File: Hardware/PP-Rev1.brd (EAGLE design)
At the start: 100 x 80 mm, 113 parts, among them IC1 LT6004, Q1 MOSFET-PCHANNEL, Q2 MOSFET-PCHANNEL, Q3 MOSFET-PCHANNEL, Q4 MOSFET-PCHANNEL, Q5 MOSFET-PCHANNEL, Q6 MOSFET-PCHANNEL, Q7 MOSFET-PCHANNEL, Q8 MOSFET-PCHANNEL, Q9 CSD18532

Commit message: Added E-Stop connectors, powersupplies (12V, 5V), additional cell tap line connector for off-board measurements
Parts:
- added C17, C18, C19, C20: 47µF, resistor:C1206
- added CELL-MEAS: 22-23-2091, con-molex:22-23-2091
- added F1: PTCSMD, SparkFun-PowerIC:PTC-1206
- added JP2, JP3: M02POLAR, SparkFun-Connectors:MOLEX-1X2
- added L2, L3: Fair-Rite 2773019447, rcl:L8530M
- added OKI-78SR: Q_OKI-78SR5, MRDT-2015-PowerBoard:OKI-78SRH
- added OKI-78SR1: Q_OKI-78SR12, MRDT-2015-PowerBoard:OKI-78SRH
- added R45, R46: 10kΩ, resistor:R1206
- added S1: (no value), SparkFun-Electromechanical:SWITCH-SPDT
- moved CHARGER+ 204.5 mm to (90.2, 11.4)
- moved U$12 178.6 mm to (40.6, 20.3)
- moved U$9 163.5 mm to (47.0, 26.7)
- moved U$11 159.1 mm to (71.1, 12.7), turned to 90 degrees
- moved Q9 155.0 mm to (57.1, 11.4), turned to 270 degrees
- moved U$4 124.4 mm to (31.8, 53.3), turned to 90 degrees
- moved U$10 123.3 mm to (72.4, 31.8), turned to 90 degrees
- moved CHARGER- 114.6 mm to (90.2, 34.3)
- moved U$5 97.1 mm to (38.1, 43.2), turned to 180 degrees
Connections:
- removed net N$32: C14.1, IRLS3034-7P.2.PAD, IRLS3034-7P.PAD, R41.2, U$2.5_1, U$2.5_10, U$2.5_11, U$2.5_12, U$2.5_13, U$2.5_14, U$2.5_15, U$2.5_16, U$2.5_2, U$2.5_3, U$2.5_4, U$2.5_5, U$2.5_6, U$2.5_7, U$2.5_8, U$2.5_9, U$2.5_B, U$2.5_T, U$4.4_1, U$4.4_10, U$4.4_11, U$4.4_12, U$4.4_13, U$4.4_14, U$4.4_15, U$4.4_16, U$4.4_2, U$4.4_3, U$4.4_4, U$4.4_5, U$4.4_6, U$4.4_7, U$4.4_8, U$4.4_9, U$4.4_B, U$4.4_T, U$8.6, U$8.8
- new net 5V: C18.1, L3.2, R45.2, R46.2
- new net ESTOP_1: JP3.2, R45.1
- new net ESTOP_2: JP2.2, R46.1
- new net LOGIC_POWER: F1.2, OKI-78SR.1, OKI-78SR1.1
- new net N$100: C17.1, L3.1, OKI-78SR.3
- new net N$33: C19.1, L2.1, OKI-78SR1.3
- new net N$41: C14.1, IRLS3034-7P.2.PAD, IRLS3034-7P.PAD, R41.2, S1.1, U$2.5_1, U$2.5_10, U$2.5_11, U$2.5_12, U$2.5_13, U$2.5_14, U$2.5_15, U$2.5_16, U$2.5_2, U$2.5_3, U$2.5_4, U$2.5_5, U$2.5_6, U$2.5_7, U$2.5_8, U$2.5_9, U$2.5_B, U$2.5_T, U$4.4_1, U$4.4_10, U$4.4_11, U$4.4_12, U$4.4_13, U$4.4_14, U$4.4_15, U$4.4_16, U$4.4_2, U$4.4_3, U$4.4_4, U$4.4_5, U$4.4_6, U$4.4_7, U$4.4_8, U$4.4_9, U$4.4_B, U$4.4_T, U$8.6, U$8.8
- new net N$42: F1.1, S1.2
- net +12V: now also C20.1, L2.2
- net CELL_1: now also CELL-MEAS.8
- net CELL_2: now also CELL-MEAS.7
- net CELL_3: now also CELL-MEAS.6
- net CELL_4: now also CELL-MEAS.5
- net CELL_5: now also CELL-MEAS.4
- net CELL_6: now also CELL-MEAS.3
- net CELL_7: now also CELL-MEAS.2
- net CELL_8: now also CELL-MEAS.1
- net GND: now also C17.2, C18.2, C19.2, C20.2, CELL-MEAS.9, JP2.1, JP3.1, OKI-78SR.2, OKI-78SR1.2, S1.3

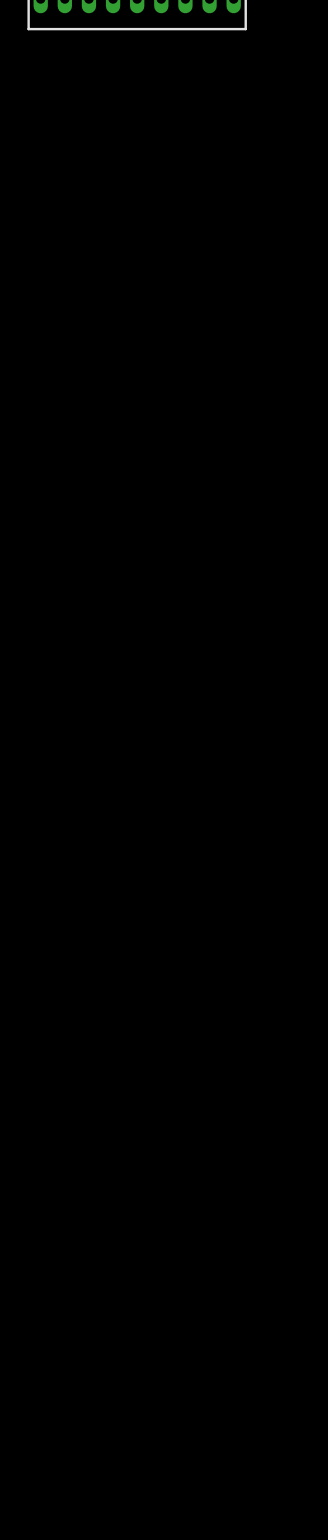
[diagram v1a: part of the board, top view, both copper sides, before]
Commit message: Fixed pull-up resistor on LED driver. Added buzzer alarms
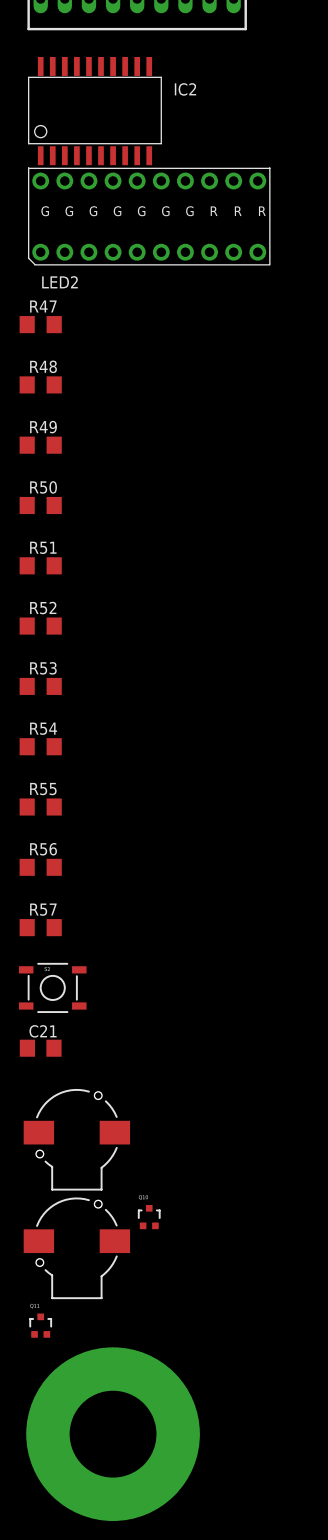
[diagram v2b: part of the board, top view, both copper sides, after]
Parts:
- added BUZZER_1, BUZZER_2: BUZZERSMD2, SparkFun-Electromechanical:BUZZER-CCV
- added C21: 0.1uF, resistor:C1206
- added IC2: TLC6C5912-Q1, 2016PowerPackLibraries:SOIC-20
- added LED2: LED-DC7G3HWA, 2016PowerPackLibraries:LED-10
- added Q10, Q11: 2N7002PW, SparkFun-DiscreteSemi:SOT323
- added R47, R48, R49, R50, R51, R52, R53, R54, R55, R56: 200R, rcl:R1206
- added R57: 10k, rcl:R1206
- added S2: SWITCH-MOMENTARY-2SMD, SparkFun-Electromechanical:TACTILE-SWITCH-SMD
- added V_OUT1: TERMINAL_HOLE, MRDT-2015-PowerBoard:LARGE_TERMINAL_HOLE
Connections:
- new net BUZZ_1: Q11.1
- new net BUZZ_2: Q10.1
- new net LED_CLR: IC2.P$9
- new net LED_RCK: IC2.P$12
- new net LED_SER_IN: IC2.P$2
- new net LED_SRCK: IC2.P$19
- new net N$32: IC2.P$3, LED2.P$20
- new net N$43: IC2.P$4, LED2.P$19
- new net N$44: IC2.P$5, LED2.P$18
- new net N$45: IC2.P$6, LED2.P$17
- new net N$46: IC2.P$7, LED2.P$16
- new net N$47: IC2.P$8, LED2.P$15
- new net N$48: IC2.P$13, LED2.P$14
- new net N$49: IC2.P$14, LED2.P$13
- new net N$50: IC2.P$15, LED2.P$12
- new net N$51: IC2.P$16, LED2.P$11
- new net N$52: LED2.P$1, R47.1
- new net N$53: LED2.P$2, R48.1
- new net N$54: LED2.P$3, R49.1
- new net N$55: LED2.P$4, R50.1
- new net N$56: LED2.P$5, R51.1
- new net N$57: LED2.P$6, R52.1
- new net N$58: LED2.P$7, R53.1
- new net N$59: LED2.P$8, R54.1
- new net N$60: LED2.P$9, R55.1
- new net N$61: LED2.P$10, R56.1
- new net N$62: IC2.P$10, R57.2, S2.3
- new net N$63: BUZZER_1.-, Q11.3
- new net N$64: BUZZER_2.+, Q10.3
- net 5V: now also BUZZER_1.+, BUZZER_2.-, C21.1, IC2.P$1, R47.2, R48.2, R49.2, R50.2, R51.2, R52.2, R53.2, R54.2, R55.2, R56.2, R57.1
- net GND: now also C21.2, IC2.P$20, Q10.2, Q11.2, S2.1, V_OUT1.P$1

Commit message: Preliminary board layout
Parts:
- moved Q11 400.9 mm to (-95.2, 151.1)
- moved Q10 389.1 mm to (-91.4, 151.1)
- moved C21 376.1 mm to (-34.3, 146.1)
- moved S2 363.0 mm to (170.2, 3.81)
- moved R57 354.4 mm to (163.8, 2.54)
- moved V_OUT1 349.3 mm to (106.7, 10.2)
- moved BUZZER_2 346.8 mm to (-87.6, 105.4)
- moved BUZZER_1 336.6 mm to (-76.2, 105.4)
- moved R56 335.3 mm to (144.8, 2.54), turned to 180 degrees
- moved R55 333.0 mm to (144.8, 5.08), turned to 180 degrees
- moved R54 330.7 mm to (144.8, 7.62), turned to 180 degrees
- moved R53 328.5 mm to (144.8, 10.2), turned to 180 degrees
- moved R52 326.3 mm to (144.8, 12.7), turned to 180 degrees
- moved IC2 324.4 mm to (163.8, 27.9), turned to 270 degrees
- moved R51 324.1 mm to (144.8, 15.2), turned to 180 degrees
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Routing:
- net CELL_1: track 0.00 -> 89.5 mm
- net CELL_2: track 0.00 -> 82.1 mm
- net CELL_3: track 0.00 -> 74.7 mm
- net GND: track 0.00 -> 69.6 mm
- net CELL_4: track 0.00 -> 67.3 mm
- net CELL_5: track 0.00 -> 59.9 mm
- net CELL_6: track 0.00 -> 52.5 mm
- net CELL_7: track 0.00 -> 45.1 mm
- added copper zone on layer 1, net CELL_8
- added copper zone on layer 1, net N$28
- added copper zone on layer 1, net N$35
- added copper zone on layer 1, net N$37
- added copper zone on layer 1, net N$39
- added copper zone on layer 1, net N$41
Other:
- board size 100 x 80 mm -> 160 x 100 mm

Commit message: Added gitignore
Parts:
- added Q12, Q13, Q14, Q15: 2N7002PW, SparkFun-DiscreteSemi:SOT323
- added X1, X2, X3, X4: 22-23-2031, con-molex:22-23-2031
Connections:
- new net FAN_CTL_1: Q12.1
- new net FAN_CTL_2: Q13.1
- new net FAN_CTL_3: Q14.1
- new net FAN_CTL_4: Q15.1
- new net FAN_TACH_1: X1.3
- new net FAN_TACH_2: X2.3
- new net FAN_TACH_3: X3.3
- new net FAN_TACH_4: X4.3
- new net N$66: Q12.3, X1.1
- new net N$70: Q13.3, X2.1
- new net N$71: Q14.3, X3.1
- new net N$72: Q15.3, X4.1
- net +12V: now also X1.2, X2.2, X3.2, X4.2
- net GND: now also Q12.2, Q13.2, Q14.2, Q15.2
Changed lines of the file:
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@@
 <?xml version="1.0" encoding="utf-8"?>
 <!DOCTYPE eagle SYSTEM "eagle.dtd">
-<eagle version="6.2">
+<eagle version="7.1.0">
 <drawing>
 <settings>
@@
 <layer number="44" name="Drills" color="7" fill="1" visible="no" active="yes"/>
 <layer number="45" name="Holes" color="7" fill="1" visible="no" active="yes"/>
-<layer number="46" name="Milling" color="3" fill="1" visible="no" active="yes"/>
+<layer number="46" name="Milling" color="3" fill="1" visible="yes" active="yes"/>
 <layer number="47" name="Measures" color="7" fill="1" visible="no" active="yes"/>
 <layer number="48" name="Document" color="7" fill="1" visible="yes" active="yes"/>
@@
 <layer number="59" name="tCarbon" color="7" fill="1" visible="no" active="no"/>
 <layer number="60" name="bCarbon" color="7" fill="1" visible="no" active="no"/>
-<layer number="90" name="Modules" color="5" fill="1" visible="yes" active="yes"/>
+<layer number="90" name="Modules" color="5" fill="1" visible="no" active="no"/>
 <layer number="91" name="Nets" color="2" fill="1" visible="no" active="no"/>
 <layer number="92" name="Busses" color="1" fill="1" visible="no" active="no"/>
@@
 </class>
 </classes>
-<designrules>
+<designrules name="default">
 <description language="de">&lt;b&gt;EAGLE Design Rules&lt;/b&gt;
 &lt;p&gt;
@@
 <pass name="Default">
 <param name="RoutingGrid" value="50mil"/>
+<param name="AutoGrid" value="1"/>
+<param name="Efforts" value="0"/>
+<param name="TopRouterVariant" value="1"/>
 <param name="tpViaShape" value="round"/>
 <param name="PrefDir.1" value="|"/>
@@
 </element>
 <element name="V_OUT1" library="MRDT-2015-PowerBoard" package="LARGE_TERMINAL_HOLE" value="TERMINAL_HOLE" x="106.68" y="10.16"/>
+<element name="X1" library="con-molex" package="22-23-2031" value="22-23-2031" x="-146.05" y="5.08">
+<attribute name="OC_NEWARK" value="30C0862" x="-146.05" y="5.08" size="1.778" layer="27" display="off"/>
+<attribute name="MPN" value="22-23-2031" x="-146.05" y="5.08" size="1.778" layer="27" display="off"/>
+<attribute name="MF" value="MOLEX" x="-146.05" y="5.08" size="1.778" layer="27" display="off"/>
+<attribute name="OC_FARNELL" value="1462950" x="-146.05" y="5.08" size="1.778" layer="27" display="off"/>
+</element>
+<element name="X2" library="con-molex" package="22-23-2031" value="22-23-2031" x="-154.94" y="5.08">
+<attribute name="OC_NEWARK" value="30C0862" x="-154.94" y="5.08" size="1.778" layer="27" display="off"/>
+<attribute name="MPN" value="22-23-2031" x="-154.94" y="5.08" size="1.778" layer="27" display="off"/>
+<attribute name="MF" value="MOLEX" x="-154.94" y="5.08" size="1.778" layer="27" display="off"/>
+<attribute name="OC_FARNELL" value="1462950" x="-154.94" y="5.08" size="1.778" layer="27" display="off"/>
+</element>
+<element name="X3" library="con-molex" package="22-23-2031" value="22-23-2031" x="-163.83" y="5.08">
+<attribute name="OC_NEWARK" value="30C0862" x="-163.83" y="5.08" size="1.778" layer="27" display="off"/>
+<attribute name="MPN" value="22-23-2031" x="-163.83" y="5.08" size="1.778" layer="27" display="off"/>
+<attribute name="MF" value="MOLEX" x="-163.83" y="5.08" size="1.778" layer="27" display="off"/>
+<attribute name="OC_FARNELL" value="1462950" x="-163.83" y="5.08" size="1.778" layer="27" display="off"/>
+</element>
+<element name="X4" library="con-molex" package="22-23-2031" value="22-23-2031" x="-172.72" y="5.08">
+<attribute name="OC_NEWARK" value="30C0862" x="-172.72" y="5.08" size="1.778" layer="27" display="off"/>
+<attribute name="MPN" value="22-23-2031" x="-172.72" y="5.08" size="1.778" layer="27" display="off"/>
+<attribute name="MF" value="MOLEX" x="-172.72" y="5.08" size="1.778" layer="27" display="off"/>
+<attribute name="OC_FARNELL" value="1462950" x="-172.72" y="5.08" size="1.778" layer="27" display="off"/>
+</element>
+<element name="Q12" library="SparkFun-DiscreteSemi" package="SOT323" value="2N7002PW" x="-179.07" y="1.27">
+<attribute name="PROD_ID" value="TRANS-11151" x="-179.07" y="1.27" size="1.778" layer="27" display="off"/>
+</element>
+<element name="Q13" library="SparkFun-DiscreteSemi" package="SOT323" value="2N7002PW" x="-182.88" y="1.27">
+<attribute name="PROD_ID" value="TRANS-11151" x="-182.88" y="1.27" size="1.778" layer="27" display="off"/>
+</element>
+<element name="Q14" library="SparkFun-DiscreteSemi" package="SOT323" value="2N7002PW" x="-186.69" y="1.27">
+<attribute name="PROD_ID" value="TRANS-11151" x="-186.69" y="1.27" size="1.778" layer="27" display="off"/>
+</element>
+<element name="Q15" library="SparkFun-DiscreteSemi" package="SOT323" value="2N7002PW" x="-190.5" y="1.27">
+<attribute name="PROD_ID" value="TRANS-11151" x="-190.5" y="1.27" size="1.778" layer="27" display="off"/>
+</element>
 </elements>
 <signals>
@@
 <wire x1="137.795" y1="79.6925" x2="137.795" y2="46.355" width="1.27" layer="16"/>
 <wire x1="137.795" y1="46.355" x2="124.46" y2="33.02" width="1.27" layer="16"/>
+<contactref element="Q12" pad="2"/>
+<contactref element="Q13" pad="2"/>
+<contactref element="Q14" pad="2"/>
+<contactref element="Q15" pad="2"/>
 <wire x1="155.575" y1="76.965" x2="155.575" y2="83.315" width="0" layer="19" extent="16-16"/>
 <wire x1="155.575" y1="70.615" x2="155.575" y2="76.965" width="0" layer="19" extent="16-16"/>
@@
 <wire x1="87.63" y1="85.09" x2="66.1" y2="46.355" width="0" layer="19" extent="1-1"/>
 <wire x1="-111.76" y1="85.09" x2="-102.74" y2="133.35" width="0" layer="19" extent="1-1"/>
+<wire x1="-178.42" y1="0.345" x2="-111.76" y2="85.09" width="0" layer="19" extent="1-1"/>
+<wire x1="-182.23" y1="0.345" x2="-178.42" y2="0.345" width="0" layer="19" extent="1-1"/>
+<wire x1="-186.04" y1="0.345" x2="-182.23" y2="0.345" width="0" layer="19" extent="1-1"/>
+<wire x1="-189.85" y1="0.345" x2="-186.04" y2="0.345" width="0" layer="19" extent="1-1"/>
 </signal>
 <signal name="N$2">
@@
 <contactref element="L2" pad="2"/>
 <contactref element="C20" pad="1"/>
+<contactref element="X1" pad="2"/>
+<contactref element="X4" pad="2"/>
+<contactref element="X3" pad="2"/>
+<contactref element="X2" pad="2"/>
+<wire x1="-163.83" y1="5.08" x2="-172.72" y2="5.08" width="0" layer="19" extent="1-1"/>
+<wire x1="-154.94" y1="5.08" x2="-163.83" y2="5.08" width="0" layer="19" extent="1-1"/>
+<wire x1="-146.05" y1="5.08" x2="-154.94" y2="5.08" width="0" layer="19" extent="1-1"/>
+<wire x1="-105.09" y1="114.47" x2="-146.05" y2="5.08" width="0" layer="19" extent="1-1"/>
+<wire x1="-134.75" y1="139.7" x2="-105.09" y2="114.47" width="0" layer="19" extent="1-1"/>
+<wire x1="57.3505" y1="35.885" x2="-105.09" y2="114.47" width="0" layer="19" extent="1-1"/>
+<wire x1="126.89" y1="8.89" x2="57.3505" y2="35.885" width="0" layer="19" extent="1-1"/>
 <wire x1="127" y1="2.41" x2="126.89" y2="8.89" width="0" layer="19" extent="1-1"/>
-<wire x1="57.3505" y1="35.885" x2="126.89" y2="8.89" width="0" layer="19" extent="1-1"/>
-<wire x1="-105.09" y1="114.47" x2="57.3505" y2="35.885" width="0" layer="19" extent="1-1"/>
-<wire x1="-134.75" y1="139.7" x2="-105.09" y2="114.47" width="0" layer="19" extent="1-1"/>
 </signal>
 <signal name="N$38">
@@
 <wire x1="167.386" y1="1.905" x2="165.252" y2="2.54" width="0" layer="19" extent="1-1"/>
 </signal>
+<signal name="N$65">
+<via x="105.41" y="78.74" extent="1-16" drill="0.6" shape="square"/>
+</signal>
+<signal name="N$66">
+<contactref element="Q12" pad="3"/>
+<contactref element="X1" pad="1"/>
+<wire x1="-148.59" y1="5.08" x2="-179.07" y2="2.195" width="0" layer="19" extent="1-1"/>
+</signal>
+<signal name="FAN_CTL_1">
+<contactref element="Q12" pad="1"/>
+</signal>
+<signal name="FAN_TACH_1">
+<contactref element="X1" pad="3"/>
+</signal>
+<signal name="N$70">
+<contactref element="Q13" pad="3"/>
+<contactref element="X2" pad="1"/>
+<wire x1="-157.48" y1="5.08" x2="-182.88" y2="2.195" width="0" layer="19" extent="1-1"/>
+</signal>
+<signal name="N$71">
+<contactref element="Q14" pad="3"/>
+<contactref element="X3" pad="1"/>
+<wire x1="-166.37" y1="5.08" x2="-186.69" y2="2.195" width="0" layer="19" extent="1-1"/>
+</signal>
+<signal name="N$72">
+<contactref element="Q15" pad="3"/>
+<contactref element="X4" pad="1"/>
+<wire x1="-175.26" y1="5.08" x2="-190.5" y2="2.195" width="0" layer="19" extent="1-1"/>
+</signal>
+<signal name="FAN_TACH_2">
+<contactref element="X2" pad="3"/>
+</signal>
+<signal name="FAN_TACH_3">
+<contactref element="X3" pad="3"/>
+</signal>
+<signal name="FAN_TACH_4">
+<contactref element="X4" pad="3"/>
+</signal>
+<signal name="FAN_CTL_4">
+<contactref element="Q15" pad="1"/>
+</signal>
+<signal name="FAN_CTL_3">
+<contactref element="Q14" pad="1"/>
+</signal>
+<signal name="FAN_CTL_2">
+<contactref element="Q13" pad="1"/>
+</signal>
 </signals>

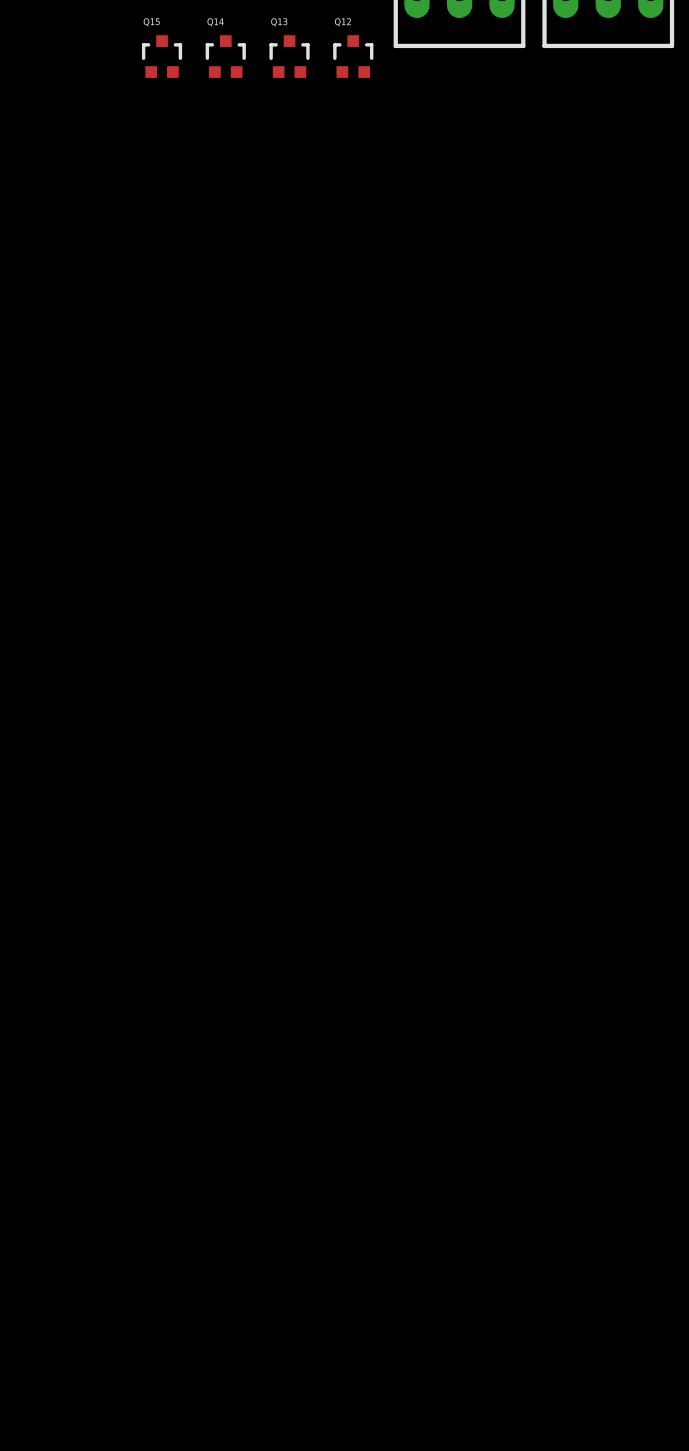
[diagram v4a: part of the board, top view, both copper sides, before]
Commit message: Add external LED Connector
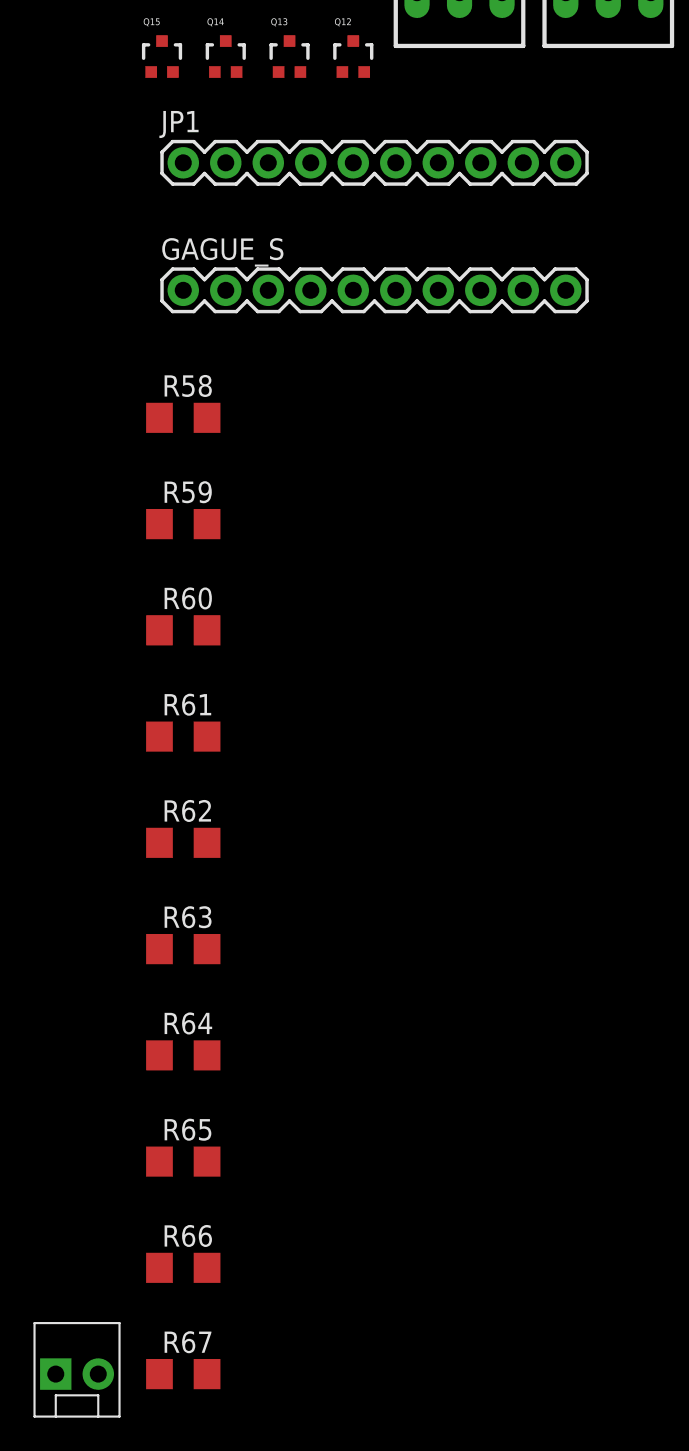
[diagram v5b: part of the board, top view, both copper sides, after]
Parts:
- added GAGUE_S, JP1: M10", SparkFun-Connectors:1X10
- added GAUGE_ON: M02POLAR, SparkFun-Connectors:MOLEX-1X2
- added R58, R59, R60, R61, R62, R63, R64, R65, R66, R67: 200R, rcl:R1206
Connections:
- removed net N$45: IC2.P$6, LED2.P$17
- new net GAUGE_D: IC2.P$6, JP1.7, LED2.P$17
- new net N$75: GAGUE_S.1, R58.2
- new net N$76: GAGUE_S.2, R59.2
- new net N$77: GAGUE_S.3, R60.2
- new net N$78: GAGUE_S.4, R61.2
- new net N$79: GAGUE_S.5, R62.2
- new net N$80: GAGUE_S.6, R63.2
- new net N$81: GAGUE_S.7, R64.2
- new net N$82: GAGUE_S.8, R65.2
- new net N$83: GAGUE_S.9, R66.2
- new net N$84: GAGUE_S.10, R67.2
- net 5V: now also R58.1, R59.1, R60.1, R61.1, R62.1, R63.1, R64.1, R65.1, R66.1, R67.1
- net GND: now also GAUGE_ON.1
- net N$32: now also JP1.10
- net N$43: now also JP1.9
- net N$44: now also JP1.8
- net N$46: now also JP1.6
- net N$47: now also JP1.5
- net N$48: now also JP1.4
- net N$49: now also JP1.3
- net N$50: now also JP1.2
- net N$51: now also JP1.1
- net N$62: now also GAUGE_ON.2
